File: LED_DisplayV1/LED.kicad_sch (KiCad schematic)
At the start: 12 parts, among them U3 TPIC6C595N

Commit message: AddComponant
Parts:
- removed C14: 0.1uF, Capacitor_SMD:C_0603_1608Metric_Pad1.08x0.95mm_HandSolder, symbol Device:C
- removed D10, D4, D5, D51, D6, D7, D8, D9: LED, symbol Device:LED
- removed R11: 10k, symbol Device:R
- removed RN1: R_Network08, Resistor_THT:R_Array_SIP9, symbol Device:R_Network08
- removed U3: TPIC6C595N, N0016A, symbol 2026-05-05_14-43-28:TPIC6C595N
- added C22: 0.1uF, Capacitor_SMD:C_0603_1608Metric_Pad1.08x0.95mm_HandSolder, symbol Device:C
- added D60, D61, D62, D63, D64, D65, D66, D67: LED, LED_THT:LED_Rectangular_W3.0mm_H2.0mm, symbol Device:LED
- added R18: 10k, Resistor_SMD:R_0402_1005Metric_Pad0.72x0.64mm_HandSolder, symbol Device:R
- added RN8: R_Network08, Resistor_THT:R_Array_SIP9, symbol Device:R_Network08
- added U10: TPIC6C595N, TPIC6C595N:N0016A, symbol 2026-05-05_14-43-28:TPIC6C595N
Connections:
- net +5V: now also C22.1, R18.1, U10.1 (VCC)
- net G: now also U10.8 (G_N)
- net GND: now also C22.2, U10.16 (GND)
- net RCK: now also U10.10 (RCK)
- net SER_IN: now also U10.2 (SER_IN)
- net SRCK: now also U10.15 (SRCK)
- net Ser_out: now also U10.9 (SER_OUT)
- net V_led: now also RN8.1 (common)
- new net: D60.1 (K), U10.3 (DRAIN0)
- new net: D60.2 (A), RN8.2 (R1)
- new net: D65.1 (K), U10.12 (DRAIN5)
- new net: D65.2 (A), RN8.7 (R6)
- new net: R18.2, U10.7 (CLR_N)
- new net: D61.1 (K), U10.4 (DRAIN1)
- new net: D61.2 (A), RN8.3 (R2)
- new net: D64.1 (K), U10.11 (DRAIN4)
- new net: D66.1 (K), U10.13 (DRAIN6)
- new net: D67.1 (K), U10.14 (DRAIN7)
- new net: D62.1 (K), U10.5 (DRAIN2)
- new net: D63.1 (K), U10.6 (DRAIN3)
- new net: D67.2 (A), RN8.9 (R8)
- new net: D62.2 (A), RN8.4 (R3)
- new net: D66.2 (A), RN8.8 (R7)
- new net: D63.2 (A), RN8.5 (R4)
- new net: D64.2 (A), RN8.6 (R5)

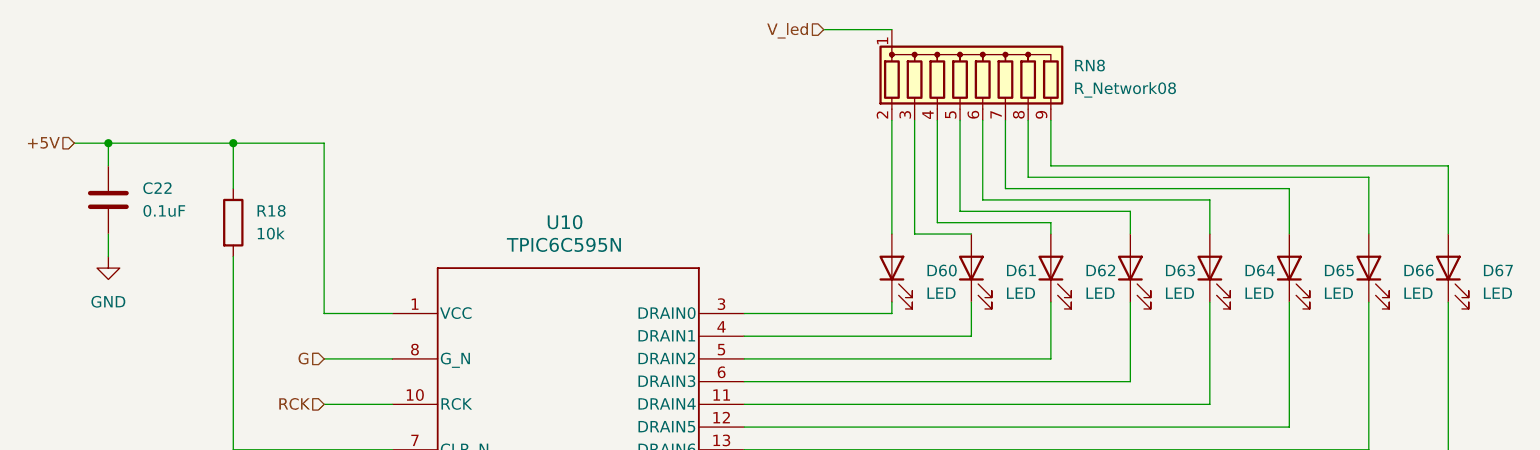
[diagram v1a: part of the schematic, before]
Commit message: Start_Routing_DisplayBoard
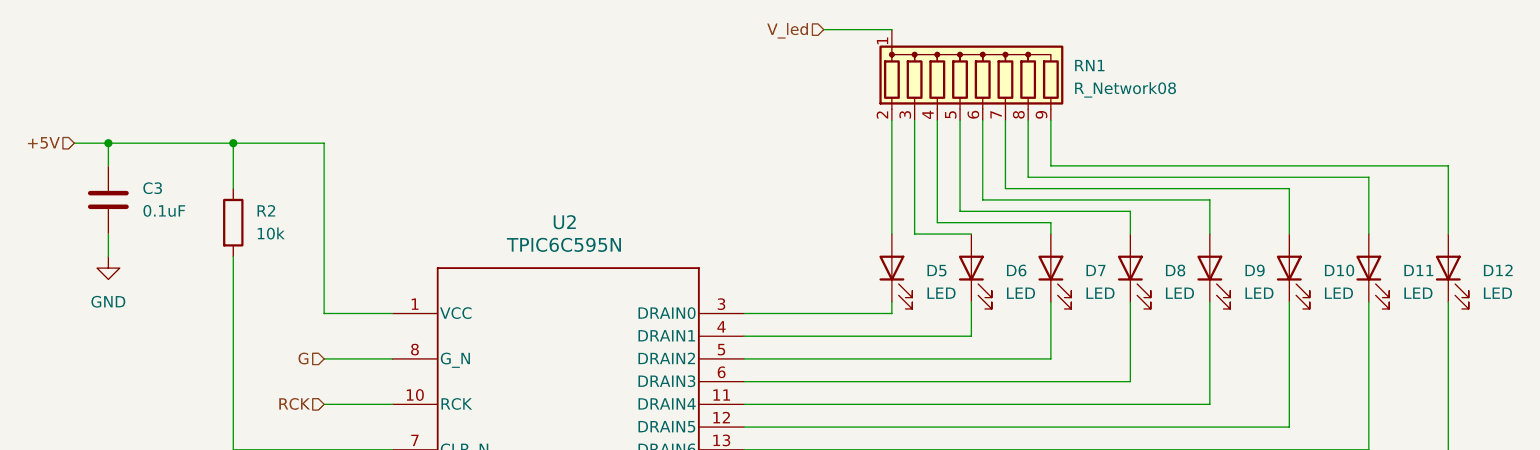
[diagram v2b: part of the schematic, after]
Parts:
- renumbered C22 to C3, D65 to D10, D66 to D11, D67 to D12, D60 to D5, D61 to D6, D62 to D7, D63 to D8, D64 to D9, R18 to R2, RN8 to RN1, U10 to U2

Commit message: All_wired
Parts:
- removed R2: 10k, Resistor_SMD:R_0402_1005Metric_Pad0.72x0.64mm_HandSolder, symbol Device:R
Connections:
- net +5V: now also U2.7 (CLR_N)
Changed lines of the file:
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@@
-	(wire
-		(pts
-			(xy 92.71 90.17) (xy 92.71 111.76)
-		)
-		(stroke
-			(width 0)
-			(type default)
-		)
-	)
 	(wire
 		(pts
@@
 	(wire
 		(pts
-			(xy 92.71 77.47) (xy 92.71 82.55)
+			(xy 92.71 77.47) (xy 92.71 111.76)
 		)
 		(stroke
@@
 					(unit 1)
 				)
-			)
-		)
-	)
-	(symbol
-		(lib_id "Device:R")
-		(at 92.71 86.36 0)
-		(unit 1)
-		(body_style 1)
-		(exclude_from_sim no)
-		(in_bom yes)
-		(on_board yes)
-		(in_pos_files yes)
-		(dnp no)
-		(fields_autoplaced yes)
-		(property "Reference" "R2"
-			(at 95.25 85.0899 0)
-			(show_name no)
-			(do_not_autoplace no)
-			(effects
-				(font
-					(size 1.27 1.27)
-				)
-				(justify left)
-			)
-		)
-		(property "Value" "10k"
-			(at 95.25 87.6299 0)
-			(show_name no)
-			(do_not_autoplace no)
-			(effects
-				(font
-					(size 1.27 1.27)
-				)
-				(justify left)
-			)
-		)
-		(property "Footprint" "Resistor_SMD:R_0402_1005Metric_Pad0.72x0.64mm_HandSolder"
-			(at 90.932 86.36 90)
-			(hide yes)
-			(show_name no)
-			(do_not_autoplace no)
-			(effects
-				(font
-					(size 1.27 1.27)
-				)
-			)
-		)
-		(property "Datasheet" ""
-			(at 92.71 86.36 0)
-			(hide yes)
-			(show_name no)
-			(do_not_autoplace no)
-			(effects
-				(font
-					(size 1.27 1.27)
-				)
-			)
-		)
-		(property "Description" "Resistor"
-			(at 92.71 86.36 0)
-			(hide yes)
-			(show_name no)
-			(do_not_autoplace no)
-			(effects
-				(font
-					(size 1.27 1.27)
-				)
-			)
-		)
-		(pin "1"
-		)
-		(pin "2"
-		)
-		(instances
-			(project "LED_DisplayV1"
-				(path "/d4a99f46-7c8c-41a4-9482-559673175209/1d038151-168f-4ffb-b417-9434b072fcd3"
-					(reference "R9")
-					(unit 1)
-				)
-				(path "/d4a99f46-7c8c-41a4-9482-559673175209/5ded5184-e2ac-49e3-930e-56cefbd0c07b"
-					(reference "R8")
-					(unit 1)
-				)
-				(path "/d4a99f46-7c8c-41a4-9482-559673175209/6c6e2f77-a520-4c33-802b-4cccb1bfc372"
-					(reference "R7")
-					(unit 1)
-				)
-				(path "/d4a99f46-7c8c-41a4-9482-559673175209/76acf5c3-ef3f-47ff-8383-3128aca97965"
-					(reference "R5")
-					(unit 1)
-				)
-				(path "/d4a99f46-7c8c-41a4-9482-559673175209/7f460fd9-69ec-437e-be33-f8a5fee7c072"
-					(reference "R6")
-					(unit 1)
-				)
-				(path "/d4a99f46-7c8c-41a4-9482-559673175209/acf7ea65-3491-4fbe-948e-6cb01756c81f"
-					(reference "R4")
-					(unit 1)
-				)
-				(path "/d4a99f46-7c8c-41a4-9482-559673175209/c1c09749-2db6-4cf0-9aa6-e152b0a77dcd"
-					(reference "R3")
-					(unit 1)
-				)
-				(path "/d4a99f46-7c8c-41a4-9482-559673175209/d42d8dce-7752-4dc1-a310-9649c32d01ec"
-					(reference "R2")
-					(unit 1)
-				)
